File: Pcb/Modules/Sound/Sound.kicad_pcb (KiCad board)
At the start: 2 copper layers, 50.8 x 20.3 mm, 15 parts, among them J1 JACK_RJ45, U1 MAX4466

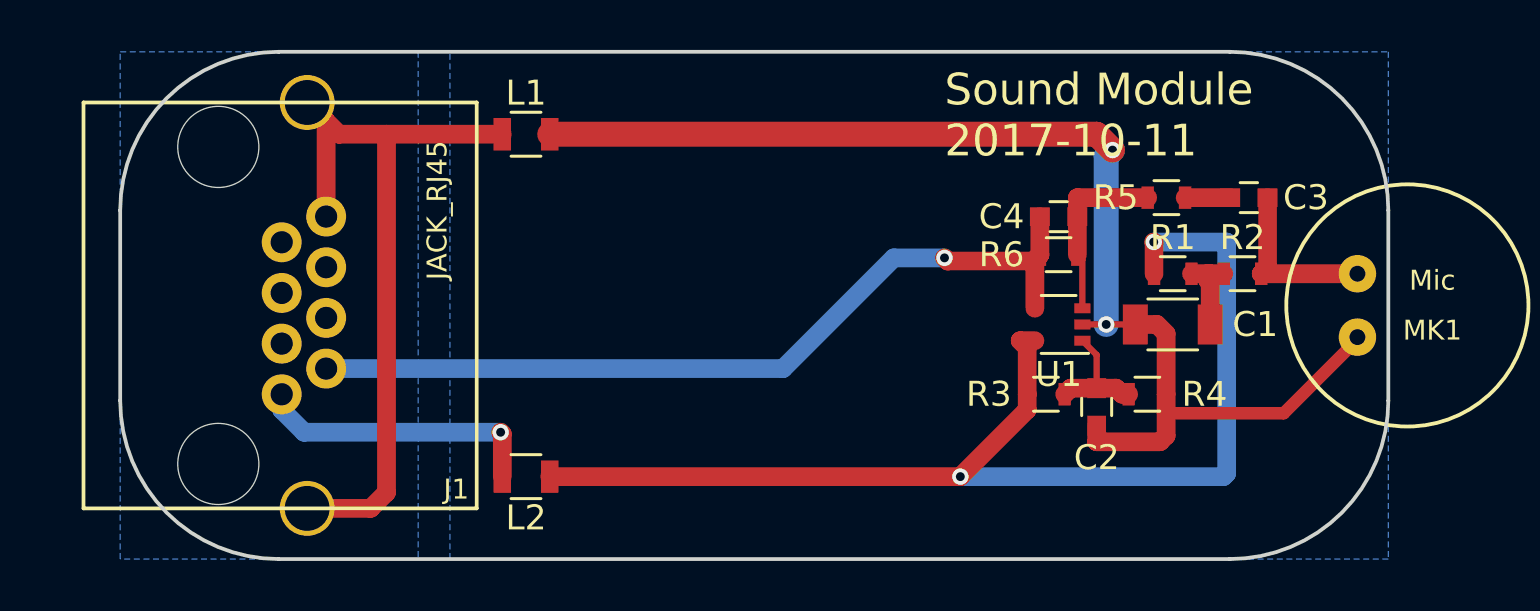
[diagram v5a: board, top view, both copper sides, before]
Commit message: Update pcb layout for modules
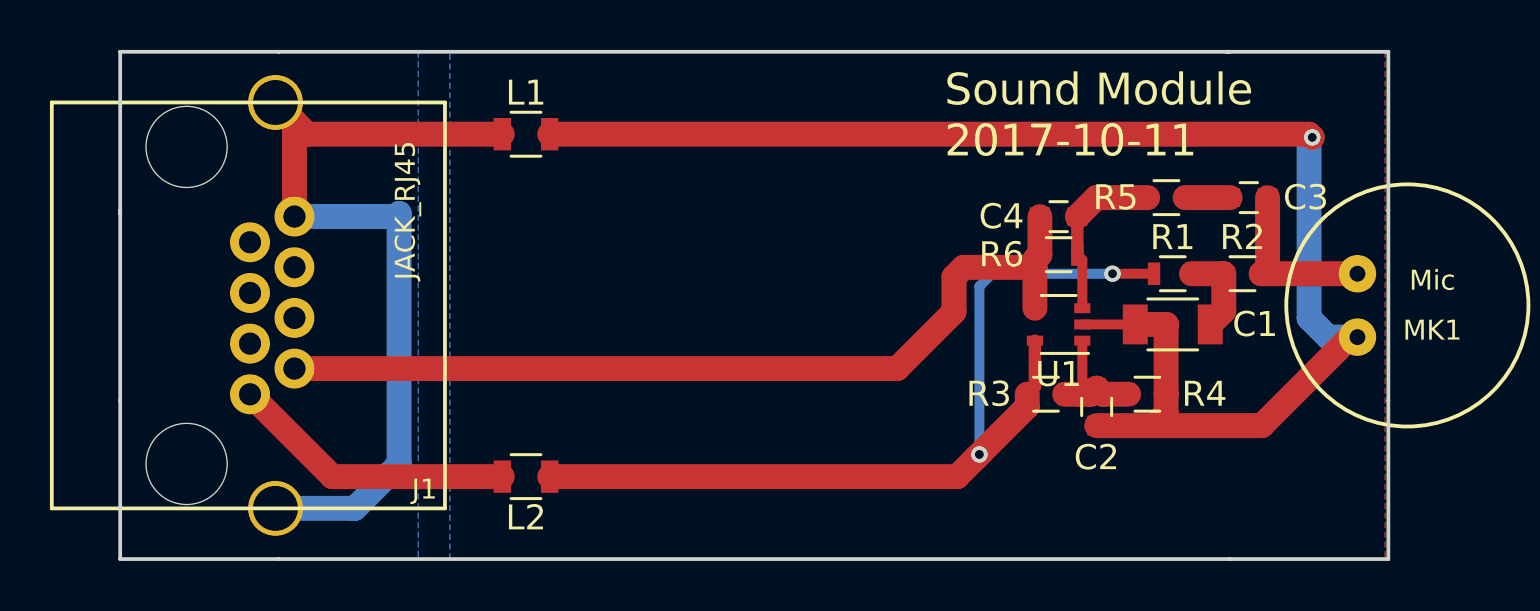
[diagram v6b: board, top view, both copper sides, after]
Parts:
- moved J1 1.27 mm to (30.5, 35.6)
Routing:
- net +3V3: track 47.9 -> 37.2 mm
- net GND: track 50.0 -> 59.7 mm, vias 2 -> 1
- net Net-(J1-Pad8): track 31.0 -> 34.5 mm
- net /AN_VAL: track 34.4 -> 35.9 mm, vias 1 -> 0
- net Net-(J1-Pad1): track 11.6 -> 11.5 mm, vias 1 -> 0
- added copper zone on F.Cu, net Net-(J1-Pad8)
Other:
- outline, holes or cut-outs redrawn
- net class Default: trace_width 1 -> 0.4

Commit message: Update PCBs
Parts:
- removed L1, L2: Ferrite_Bead, Resistors_SMD:R_0805
- added C5: 47uF, Capacitors_SMD:C_1206, F.Cu at (50.5, 40.6)
- added X1: HOLE, Mounting_Holes:MountingHole_2.5mm_Pad, F.Cu at (41.9, 28.6)
- added X2: HOLE, Mounting_Holes:MountingHole_2.5mm_Pad, F.Cu at (41.9, 42.5)
- added X3: HOLE, Mounting_Holes:MountingHole_2.5mm_Pad, F.Cu at (59.7, 28.6)
- added X4: HOLE, Mounting_Holes:MountingHole_2.5mm_Pad, F.Cu at (59.7, 42.5)
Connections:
- J1 pad 1: Net-(J1-Pad1) -> +3V3
- J1 pad 8: Net-(J1-Pad8) -> GND
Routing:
- net GND: track 59.7 -> 6.48 mm, vias 1 -> 5
- net Net-(J1-Pad8): track 34.5 -> 0.00 mm
- net +3V3: track 37.2 -> 65.6 mm
- net Net-(J1-Pad1): track 11.5 -> 0.00 mm
- net /AN_VAL: track 35.9 -> 34.4 mm
- removed copper zone on B.Cu, net Net-(J1-Pad8)
- removed copper zone on F.Cu, net Net-(J1-Pad8)
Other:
- net class Default: trace_width 0.4 -> 0.254
- board text added: "Sound Module 2017-12-03"
- board text removed: "Sound Module 2017-10-11"

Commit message: Update pcbs.
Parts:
- moved MK1 0.25 mm to (77.2, 35.6)
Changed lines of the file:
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@@
   )
   (setup
-    (last_trace_width 0.381)
+    (last_trace_width 0.254)
     (user_trace_width 0.381)
     (user_trace_width 0.508)
@@
   )
   (module CA6:MIC_CMA-4544PF (layer F.Cu)
-    (at 76.962 35.56 180)
+    (at 77.216 35.56 180)
     (tags "CMS SM")
     (attr smd)
